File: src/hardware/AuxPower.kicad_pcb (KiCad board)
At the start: 2 copper layers, 90 x 90 mm, 104 parts, among them J1 MC 1,5/2, J10 MC 1,5/4, J11 S3B-XH-A, J12 S3B-XH-A, J13 S3B-XH-A, J14 S3B-XH-A, J15 S3B-XH-A, J16 B3B-XH-A, J17 B4B-XH-A, J2 MC 1,5/2, J3 MC 1,5/2, J4 MC 1,5/2, J5 MC 1,5/2, J6 MC 1,5/4, J7 MC 1,5/4, J8 MC 1,5/4, J9 MC 1,5/4, K1 AQZ202G, K2 AQZ202G, K3 AQZ202G, K4 AQZ202G, K5 AQZ202G, U1 ZXCT1009, U2 ZXCT1009, U3 ZXCT1009, U4 ZXCT1009, U5 ZXCT1009, U6 PIC18F26K83, U7 PI4IOE5V6416, U8 MCP9701

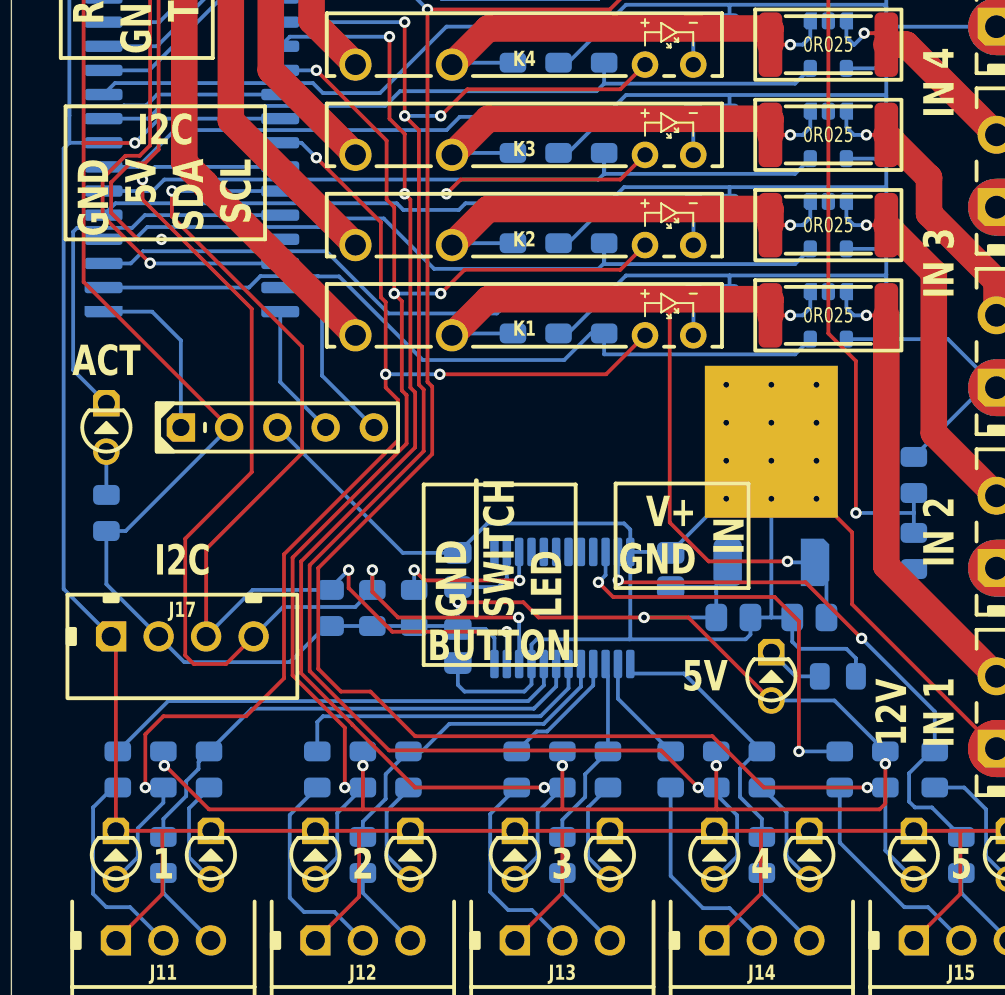
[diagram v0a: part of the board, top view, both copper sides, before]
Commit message: Fixed output LEDS
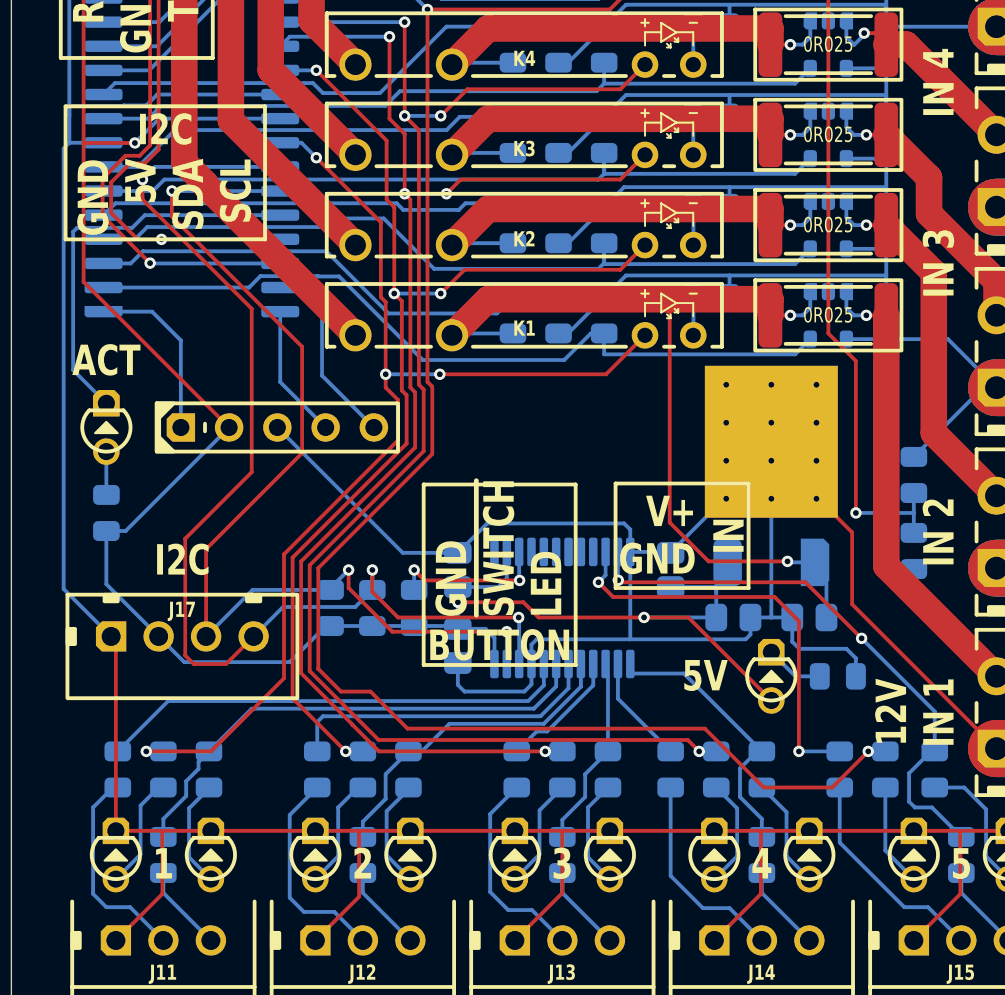
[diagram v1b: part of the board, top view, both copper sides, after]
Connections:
- DS10 pad 2: OUT_OUTPUT5 -> LED_OUTPUT5
- DS6 pad 2: OUT_OUTPUT1 -> LED_OUTPUT1
- DS7 pad 2: OUT_OUTPUT2 -> LED_OUTPUT2
- DS8 pad 2: OUT_OUTPUT3 -> LED_OUTPUT3
- DS9 pad 2: OUT_OUTPUT4 -> LED_OUTPUT4
- R22 pad 1: 5V -> OUT_OUTPUT1
- R22 pad 2: OUT_OUTPUT1 -> LED_OUTPUT1
- R23 pad 1: 5V -> OUT_OUTPUT2
- R23 pad 2: OUT_OUTPUT2 -> LED_OUTPUT2
- R24 pad 1: 5V -> OUT_OUTPUT3
- R24 pad 2: OUT_OUTPUT3 -> LED_OUTPUT3
- R25 pad 1: 5V -> OUT_OUTPUT4
- R25 pad 2: OUT_OUTPUT4 -> LED_OUTPUT4
- R26 pad 1: 5V -> OUT_OUTPUT5
- R26 pad 2: OUT_OUTPUT5 -> LED_OUTPUT5
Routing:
- net 5V: track 249.7 -> 190.7 mm, vias 9 -> 4
- net OUT_OUTPUT1: track 66.6 -> 57.2 mm
- net OUT_OUTPUT2: track 66.6 -> 58.7 mm
- net OUT_OUTPUT3: track 78.1 -> 71.4 mm
- net OUT_OUTPUT4: track 86.8 -> 80.5 mm
- net LED_OUTPUT2: track 0.00 -> 6.00 mm
- net LED_OUTPUT1: track 0.00 -> 6.00 mm
- net LED_OUTPUT3: track 0.00 -> 5.86 mm
- net LED_OUTPUT4: track 0.00 -> 5.77 mm
- net OUT_OUTPUT5: track 96.5 -> 90.8 mm
- net LED_OUTPUT5: track 0.00 -> 5.44 mm

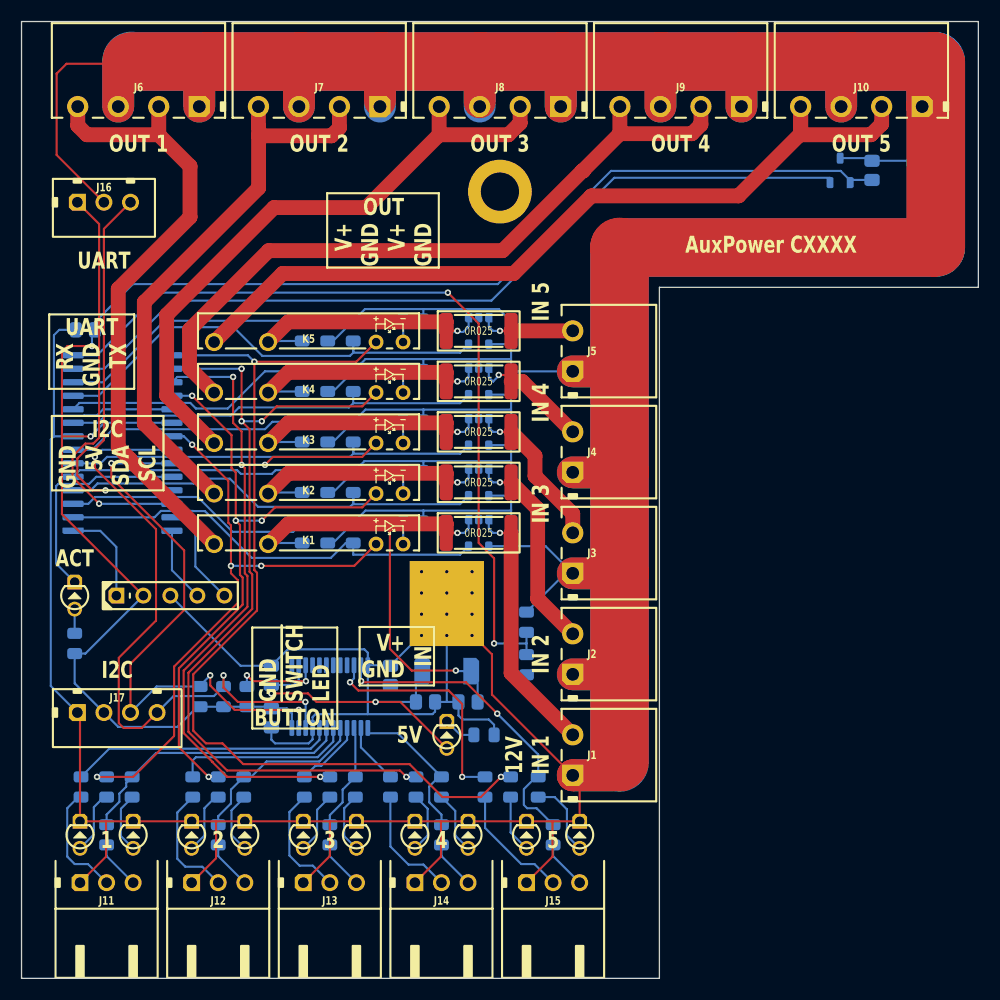
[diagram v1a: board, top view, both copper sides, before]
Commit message: Made compatible with CPC1706Y
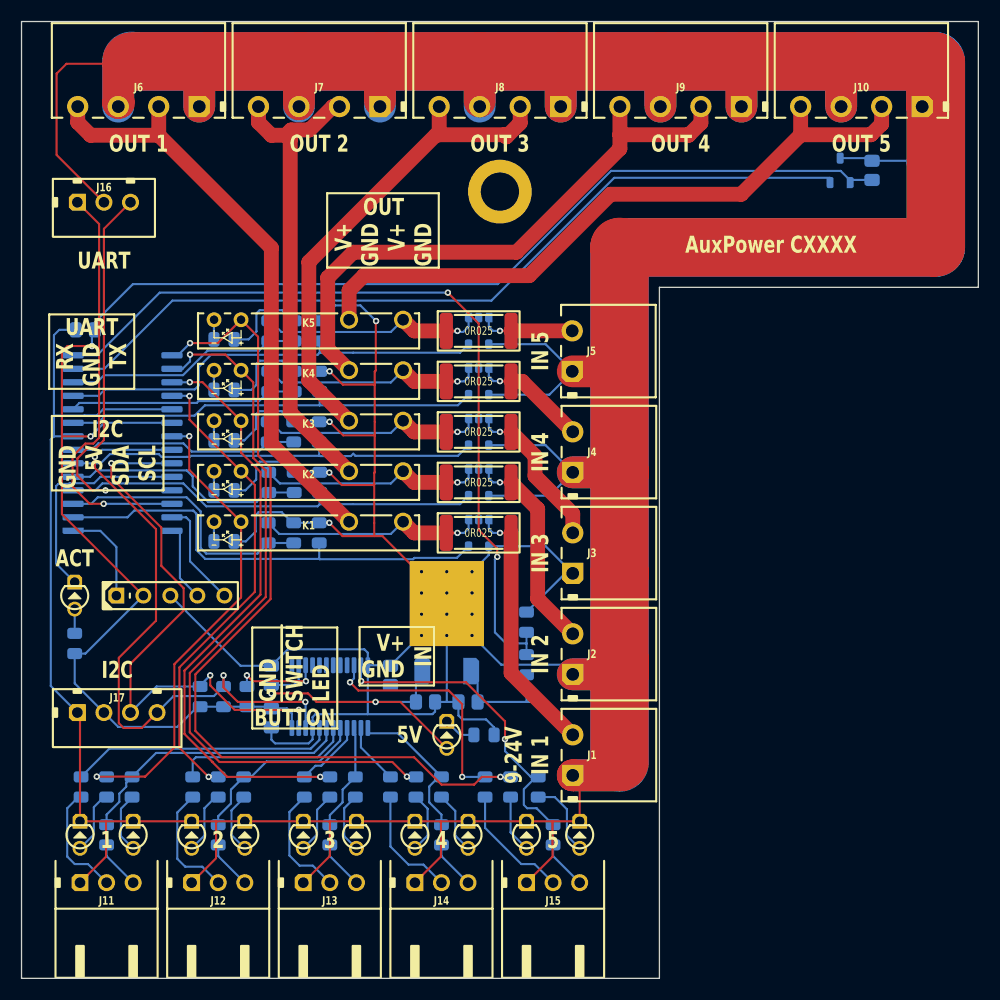
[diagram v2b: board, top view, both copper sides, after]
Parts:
- moved R16 17.9 mm to (34.0, 63.9)
- moved R18 17.9 mm to (34.0, 54.4)
- moved R19 17.9 mm to (34.0, 49.6)
- moved R20 17.9 mm to (34.0, 44.9)
- moved R17 17.9 mm to (34.0, 59.1)
- moved R11 3.20 mm to (43.0, 63.1)
- moved R13 3.20 mm to (43.0, 53.6)
- moved R41 3.20 mm to (40.6, 63.1), turned to 90 degrees
- moved R43 3.20 mm to (40.6, 53.6), turned to 90 degrees
- moved R48 3.20 mm to (38.2, 63.1), turned to 90 degrees
- moved R50 3.20 mm to (38.2, 53.6), turned to -90 degrees
- moved R12 3.15 mm to (43.0, 58.4)
- moved R14 3.15 mm to (43.0, 48.9)
- moved R15 3.15 mm to (43.0, 44.1)
- moved R42 3.15 mm to (40.6, 58.4), turned to 90 degrees
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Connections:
- C7 pad 2: INPUT1' -> INPUT1
- K1 pad 3: INPUT1' -> OUTPUT1
- K1 pad 4: OUTPUT1 -> INPUT1'
- K2 pad 3: INPUT2' -> OUTPUT2
- K2 pad 4: OUTPUT2 -> INPUT2'
- K3 pad 3: INPUT3' -> OUTPUT3
- K3 pad 4: OUTPUT3 -> INPUT3'
- K4 pad 3: INPUT4' -> OUTPUT4
- K4 pad 4: OUTPUT4 -> INPUT4'
- K5 pad 3: INPUT5' -> OUTPUT5
- K5 pad 4: OUTPUT5 -> INPUT5'
- VR1 pad 1: INPUT1' -> INPUT1
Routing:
- net INPUT1': track 47.3 -> 21.2 mm, vias 2 -> 1
- net OUT_OUTPUT3: track 71.4 -> 56.5 mm, vias 4 -> 2
- net OUTPUT5: track 78.2 -> 63.6 mm
- net OUT_OUTPUT2: track 58.7 -> 45.0 mm, vias 4 -> 2
- net OUTPUT3: track 58.9 -> 46.1 mm
- net OUT_OUTPUT1: track 57.2 -> 44.9 mm, vias 4 -> 2
- net OUTPUT4: track 67.2 -> 55.7 mm
- net OUT_OUTPUT4: track 80.5 -> 69.0 mm, vias 4 -> 2
- net OUTPUT2: track 53.5 -> 44.8 mm
- net OUT_OUTPUT5: track 90.8 -> 82.1 mm
- net INPUT1: track 31.8 -> 39.5 mm
- net ADC_VOLTAGE4: track 25.9 -> 21.5 mm
- net GND: track 871.1 -> 866.9 mm, vias 0 -> 5
- net ADC_VOLTAGE5: track 26.3 -> 22.4 mm
- net INPUT4': track 24.6 -> 21.0 mm
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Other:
- board text added: "9-24V"
- board text removed: "12V"

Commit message: Cleanup a bit
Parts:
- moved R11 5.30 mm to (48.3, 63.1)
- moved R13 5.30 mm to (48.3, 53.6)
- moved R12 5.25 mm to (48.3, 58.4)
- moved R14 5.25 mm to (48.3, 48.9)
- moved R15 5.25 mm to (48.3, 44.1)
- moved R48 4.80 mm to (43.0, 63.1)
- moved R50 4.80 mm to (43.0, 53.6)
- moved R49 4.75 mm to (43.0, 58.4)
- moved R51 4.75 mm to (43.0, 48.9)
- moved R52 4.75 mm to (43.0, 44.1)
- moved R16 4.23 mm to (38.2, 63.1), turned to 90 degrees
- moved R18 4.23 mm to (38.2, 53.6), turned to -90 degrees
- moved R19 4.23 mm to (38.2, 48.9), turned to -90 degrees
- moved R20 4.23 mm to (38.2, 44.1), turned to -90 degrees
- moved R17 4.22 mm to (38.2, 58.4), turned to -90 degrees
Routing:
- net GND: track 866.9 -> 846.8 mm
- net INPUT1': track 21.2 -> 16.4 mm
- net INPUT2': track 21.2 -> 16.4 mm
- net INPUT5': track 21.4 -> 16.8 mm
- net INPUT3': track 21.1 -> 16.5 mm
- net INPUT4': track 21.0 -> 16.4 mm
- net OUT_OUTPUT2': track 1.79 -> 5.92 mm
- net OUT_OUTPUT5': track 1.84 -> 5.92 mm
- net OUT_OUTPUT4': track 1.84 -> 5.92 mm
- net OUT_OUTPUT3': track 1.84 -> 5.92 mm
- net OUT_OUTPUT1': track 1.84 -> 5.92 mm
- net ADC_VOLTAGE2: track 23.0 -> 25.6 mm
- net ADC_VOLTAGE3: track 21.7 -> 24.1 mm
- net ADC_VOLTAGE4: track 21.5 -> 23.8 mm
- net ADC_VOLTAGE5: track 22.4 -> 24.8 mm
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
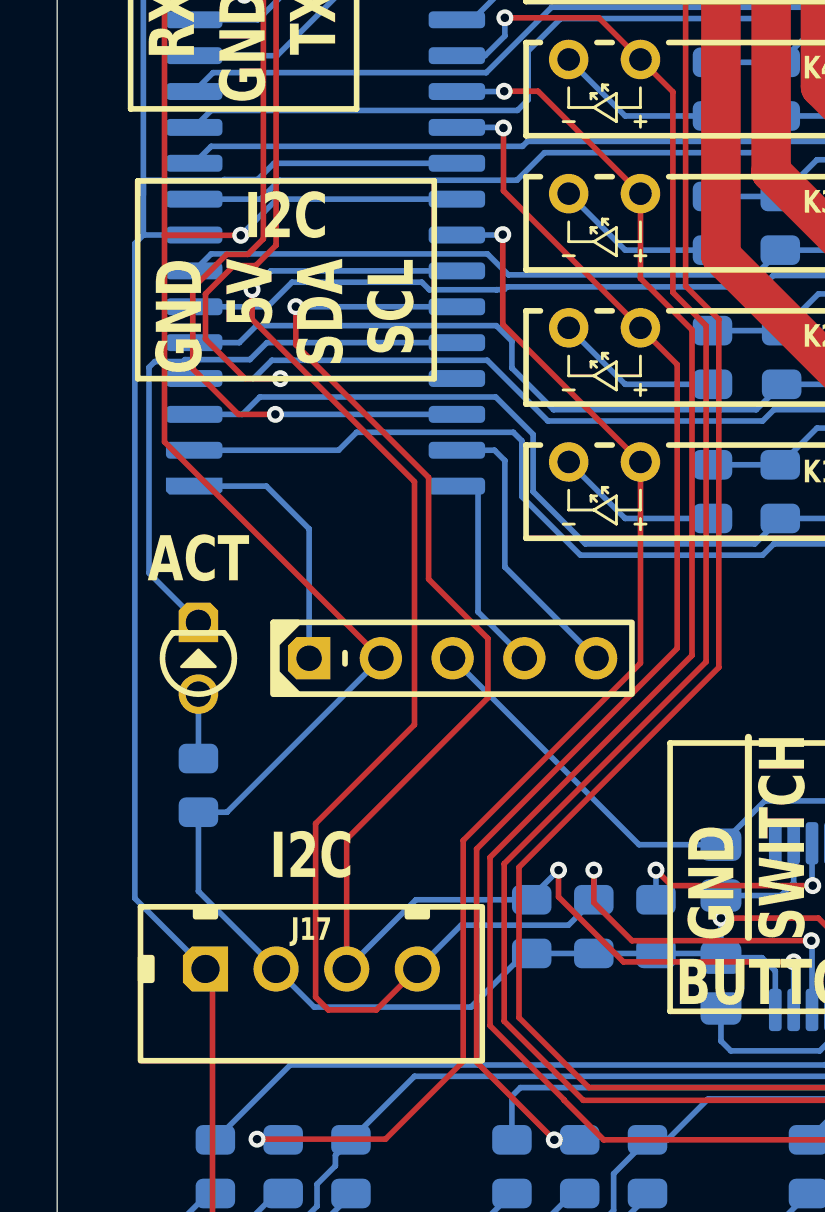
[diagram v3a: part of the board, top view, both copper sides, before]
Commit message: Swapped OLED pinout to match 128x64 order
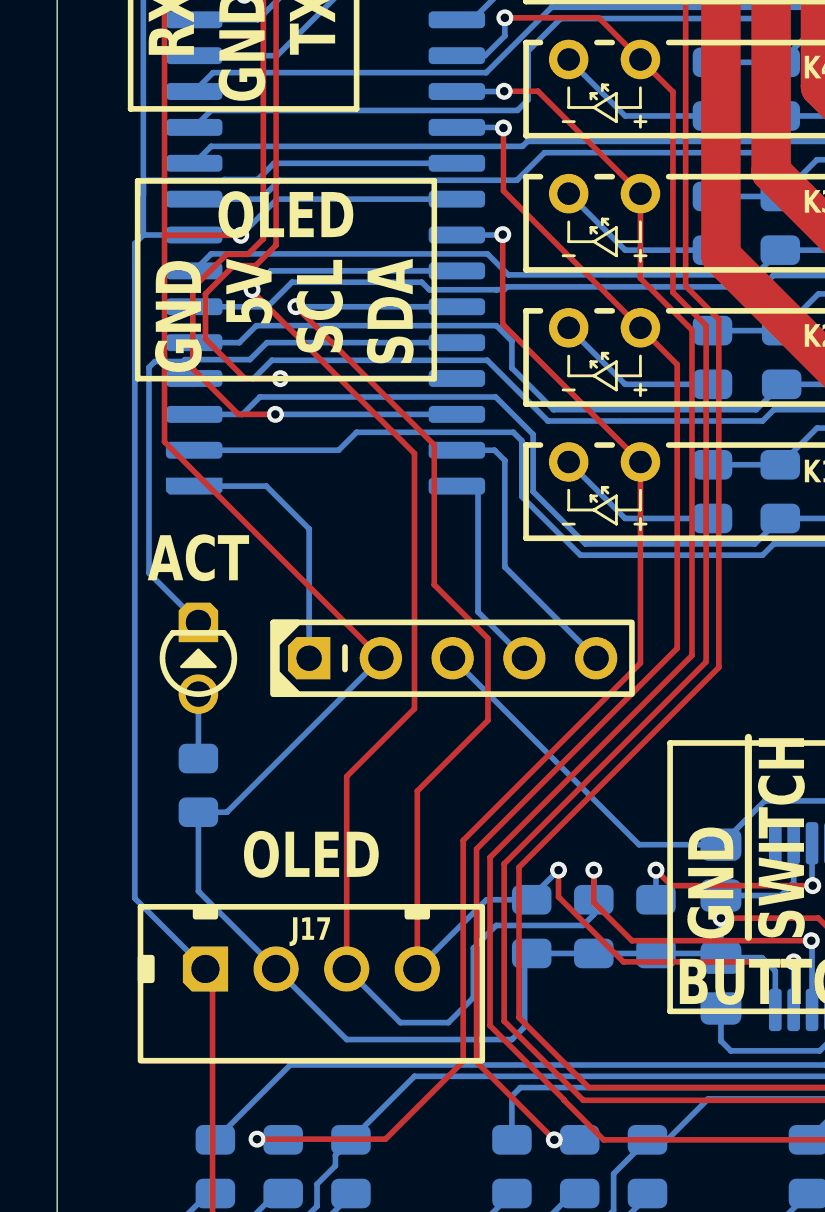
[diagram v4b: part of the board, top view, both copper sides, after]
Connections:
- J17 pad 3: I2C_SDA -> I2C_SCL
- J17 pad 4: I2C_SCL -> I2C_SDA
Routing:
- net I2C_SDA: track 54.9 -> 51.3 mm
- net 5V: track 190.7 -> 193.2 mm
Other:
- board text added: "OLED"
- board text removed: "I2C"
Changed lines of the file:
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@@
 		(attr through_hole)
 		(fp_line
-			(start -3.81 -0.2)
-			(end -3.81 0.2)
+			(start -3.81 -0.4)
+			(end -3.81 0.4)
 			(stroke
 				(width 0.2)
-				(type default)
+				(type solid)
 			)
 			(layer "F.SilkS")
@@
 			(layers "*.Cu" "*.Mask")
 			(remove_unused_layers no)
-			(net 57 "I2C_SDA")
+			(net 56 "I2C_SCL")
 		)
 		(pad "4" thru_hole circle
@@
 			(layers "*.Cu" "*.Mask")
 			(remove_unused_layers no)
-			(net 56 "I2C_SCL")
+			(net 57 "I2C_SDA")
 		)
 		(embedded_fonts no)
@@
 		)
 	)
-	(gr_text "SDA"
+	(gr_text "SCL"
 		(at 24.35 54.85 90)
 		(layer "F.SilkS")
@@
 		)
 	)
-	(gr_text "SCL"
+	(gr_text "SDA"
 		(at 26.85 54.85 90)
 		(layer "F.SilkS")
@@
 		)
 	)
-	(gr_text "I2C"
+	(gr_text "OLED"
 		(at 24 76 0)
 		(layer "F.SilkS" knockout)
@@
 		)
 	)
-	(gr_text "I2C"
+	(gr_text "OLED"
 		(at 23.1 53.35 0)
 		(layer "F.SilkS" knockout)
@@
 	)
 	(segment
-		(start 22.75 80)
-		(end 24.1 81.35)
-		(width 0.2)
-		(layer "B.Cu")
-		(net 55)
-	)
-	(segment
-		(start 29.65 81.35)
-		(end 31.55 79.45)
+		(start 25.25 82.5)
+		(end 31.1 82.5)
 		(width 0.2)
 		(layer "B.Cu")
@@
 	)
 	(segment
+		(start 31.1 82.5)
+		(end 31.55 82.05)
+		(width 0.2)
+		(layer "B.Cu")
+		(net 55)
+	)
+	(segment
 		(start 20 77.25)
 		(end 22.75 80)
@@
 	)
 	(segment
+		(start 22.75 80)
+		(end 25.25 82.5)
+		(width 0.2)
+		(layer "B.Cu")
+		(net 55)
+	)
+	(segment
 		(start 59.8 39.7)
 		(end 25.475 39.7)
@@
 	)
 	(segment
+		(start 31.55 82.05)
+		(end 31.55 79.45)
+		(width 0.2)
+		(layer "B.Cu")
+		(net 55)
+	)
+	(segment
 		(start 52.1 79)
 		(end 48.3 79)
@@
 	)
 	(segment
-		(start 24.1 81.35)
-		(end 29.65 81.35)
-		(width 0.2)
-		(layer "B.Cu")
-		(net 55)
-	)
-	(segment
 		(start 70.45 29.05)
 		(end 59.8 39.7)
@@
 	)
 	(segment
-		(start 27.75 80)
-		(end 26.3 81.45)
+		(start 27.65 70.784314)
+		(end 27.65 61.75)
 		(width 0.2)
 		(layer "F.Cu")
@@
 	)
 	(segment
-		(start 27.65 62.75)
-		(end 21.9 57)
-		(width 0.2)
-		(layer "F.Cu")
-		(net 56)
-	)
-	(segment
-		(start 26.3 81.45)
-		(end 24.6 81.45)
-		(width 0.2)
-		(layer "F.Cu")
-		(net 56)
-	)
-	(segment
-		(start 21.9 57)
-		(end 21.9 55.95)
+		(start 25.25 73.184314)
+		(end 27.65 70.784314)
 		(width 0.2)
 		(layer "F.Cu")
@@
 	)
 	(segment
-		(start 27.65 71.35)
-		(end 27.65 62.75)
+		(start 25.25 80)
+		(end 25.25 73.184314)
 		(width 0.2)
 		(layer "F.Cu")
@@
 	)
 	(segment
-		(start 24.149 74.851)
-		(end 27.65 71.35)
-		(width 0.2)
-		(layer "F.Cu")
-		(net 56)
-	)
-	(segment
-		(start 24.149 80.999)
-		(end 24.149 74.851)
+		(start 21.9 56)
+		(end 21.9 55.95)
 		(width 0.2)
 		(layer "F.Cu")
@@
 	)
 	(segment
-		(start 24.6 81.45)
-		(end 24.149 80.999)
+		(start 27.65 61.75)
+		(end 21.9 56)
 		(width 0.2)
 		(layer "F.Cu")
@@
 	)
 	(segment
+		(start 30.540743 78.459257)
+		(end 33.615743 78.459257)
+		(width 0.2)
+		(layer "B.Cu")
+		(net 56)
+	)
+	(segment
 		(start 41.725 79.025)
 		(end 41.7 79)
@@
 	)
 	(segment
+		(start 34 78.075)
+		(end 34 77.55)
+		(width 0.2)
+		(layer "B.Cu")
+		(net 56)
+	)
+	(segment
+		(start 28.85 81.9)
+		(end 29.734257 81.015743)
+		(width 0.2)
+		(layer "B.Cu")
+		(net 56)
+	)
+	(segment
+		(start 33.615743 78.459257)
+		(end 34 78.075)
+		(width 0.2)
+		(layer "B.Cu")
+		(net 56)
+	)
+	(segment
 		(start 41.725 81.45)
 		(end 41.725 79.025)
@@
 	)
 	(segment
-		(start 29.3 78.45)
-		(end 33.1 78.45)
+		(start 25.25 80)
+		(end 27.15 81.9)
 		(width 0.2)
 		(layer "B.Cu")
@@
 	)
 	(segment
-		(start 33.1 78.45)
-		(end 34 77.55)
+		(start 27.15 81.9)
+		(end 28.85 81.9)
 		(width 0.2)
 		(layer "B.Cu")
@@
 	)
 	(segment
-		(start 27.75 80)
-		(end 29.3 78.45)
+		(start 29.734257 79.265743)
+		(end 30.540743 78.459257)
 		(width 0.2)
 		(layer "B.Cu")
@@
 	)
 	(segment
+		(start 29.734257 81.015743)
+		(end 29.734257 79.265743)
+		(width 0.2)
+		(layer "B.Cu")
+		(net 56)
+	)
+	(segment
 		(start 34 77.55)
 		(end 34 76.5)
@@
 	)
 	(segment
-		(start 30.25 70.4)
-		(end 25.25 75.4)
+		(start 27.75 73.7)
+		(end 30.25 71.2)
 		(width 0.2)
 		(layer "F.Cu")
@@
 	)
 	(segment
-		(start 35.05 79.75)
-		(end 32.75 77.45)
+		(start 30.25 68.3)
+		(end 28.35 66.4)
 		(width 0.2)
 		(layer "F.Cu")
@@
 	)
 	(segment
-		(start 30.25 68.3)
-		(end 30.25 70.4)
+		(start 35.05 79.75)
+		(end 32.75 77.45)
 		(width 0.2)
 		(layer "F.Cu")
@@
 	)
 	(segment
-		(start 25.25 75.4)
-		(end 25.25 80)
-		(width 0.2)
-		(layer "F.Cu")
-		(net 57)
-	)
-	(segment
-		(start 32.75 77.45)
-		(end 32.75 76.5)
+		(start 30.25 71.2)
+		(end 30.25 68.3)
 		(width 0.2)
 		(layer "F.Cu")
@@
 	)
 	(segment
-		(start 28.15 62.6)
-		(end 28.15 66.2)
+		(start 28.35 61.45)
+		(end 23.45 56.55)
 		(width 0.2)
 		(layer "F.Cu")
@@
 	)
 	(segment
-		(start 28.15 66.2)
-		(end 30.25 68.3)
+		(start 32.75 77.45)
+		(end 32.75 76.5)
 		(width 0.2)
 		(layer "F.Cu")
@@
 	)
 	(segment
-		(start 23.45 57.9)
-		(end 28.15 62.6)
+		(start 28.35 66.4)
+		(end 28.35 61.45)
 		(width 0.2)
 		(layer "F.Cu")
@@
 	)
 	(segment
-		(start 23.45 56.55)
-		(end 23.45 57.9)
+		(start 27.75 80)
+		(end 27.75 73.7)
 		(width 0.2)
 		(layer "F.Cu")
@@
 	)
 	(segment
-		(start 23.455 56.555)
-		(end 23.45 56.55)
+		(start 27.75 80)
+		(end 30.2 77.55)
 		(width 0.2)
 		(layer "B.Cu")
@@
 	)
 	(segment
-		(start 27.7 77.55)
-		(end 31.8 77.55)
+		(start 23.455 56.555)
+		(end 23.45 56.55)
 		(width 0.2)
 		(layer "B.Cu")
@@
 	)
 	(segment
-		(start 29.15 56.555)
-		(end 23.455 56.555)
+		(start 30.2 77.55)
+		(end 31.8 77.55)
 		(width 0.2)
 		(layer "B.Cu")
@@
 	)
 	(segment
-		(start 25.25 80)
-		(end 27.7 77.55)
+		(start 29.15 56.555)
+		(end 23.455 56.555)
 		(width 0.2)
 		(layer "B.Cu")
